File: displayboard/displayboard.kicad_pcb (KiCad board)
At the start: 2 copper layers, 103 x 41 mm, 2 parts, among them P2 CONN_01X08, P3 CONN_01X08

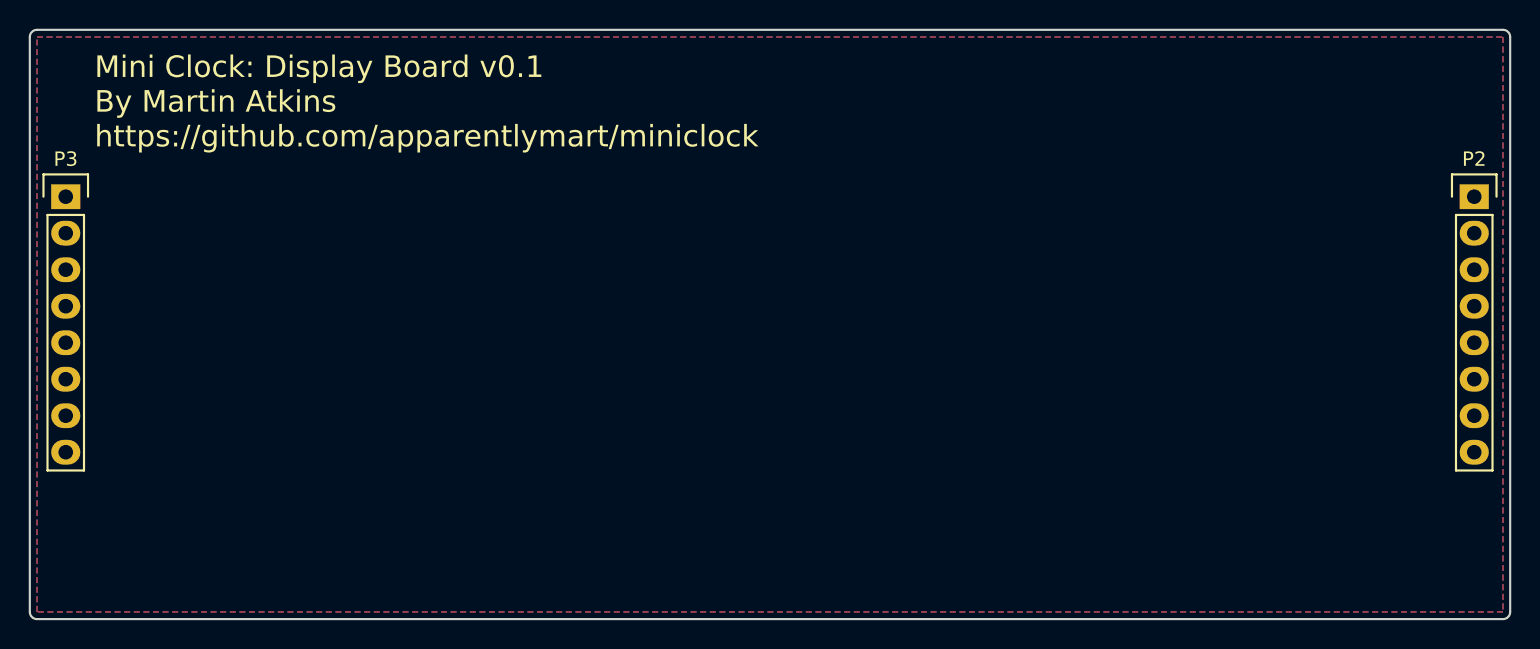
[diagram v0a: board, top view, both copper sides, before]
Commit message: PCB footprint assignment and floor planning.
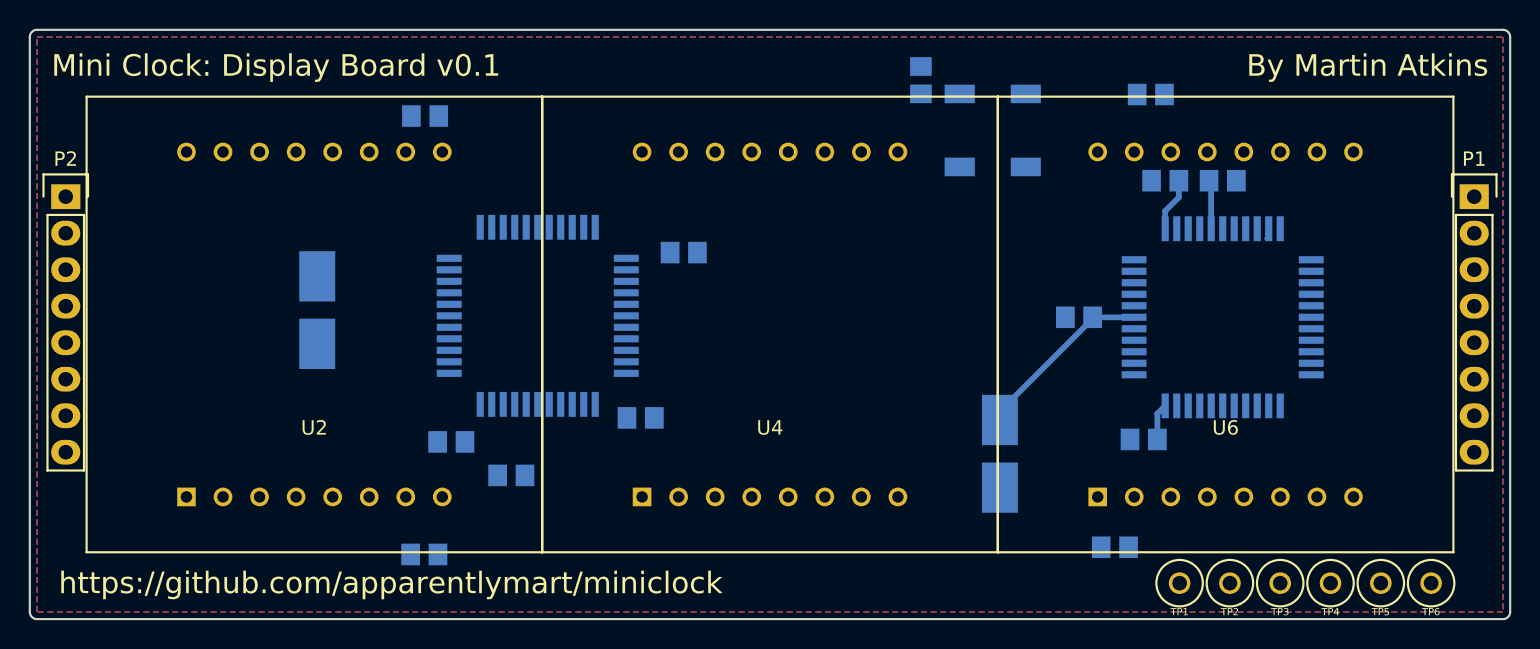
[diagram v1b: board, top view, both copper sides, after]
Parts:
- added C1: 0.1u, miniclock:0805, B.Cu at (10.5, -17.0)
- added C10: 0.1u, miniclock:0805, B.Cu at (26.0, 8.00)
- added C11: 47uF, miniclock:UWX1V470MCL1GB, B.Cu at (16.0, 9.00)
- added C2: 0.1u, miniclock:0805, B.Cu at (-22.2, 8.17)
- added C3: 0.1u, miniclock:0805, B.Cu at (-18.0, 10.5)
- added C4: 0.1u, miniclock:0805, B.Cu at (-6.00, -5.00)
- added C5: 0.1u, miniclock:0805, B.Cu at (-9.00, 6.50)
- added C6: 47uF, miniclock:UWX1V470MCL1GB, B.Cu at (-31.5, -1.00)
- added C7: 0.1u, miniclock:0805, B.Cu at (31.5, -10.0)
- added C8: 0.1u, miniclock:0805, B.Cu at (21.5, -0.50)
- added C9: 0.1u, miniclock:0805, B.Cu at (27.5, -10.0)
- added JP1: Jumper_NO_Small, miniclock:0805, B.Cu at (-24.1, 16.0)
- added JP2: Jumper_NO_Small, miniclock:0805, B.Cu at (-24.0, -14.5)
- added JP3: Jumper_NO_Small, miniclock:0805, B.Cu at (24.0, 15.5)
- added JP4: Jumper_NO_Small, miniclock:0805, B.Cu at (26.5, -16.0)
- added TP1: TESTPOINT, miniclock:TESTPOINT, F.Cu at (28.5, 18.0)
- added TP2: TESTPOINT, miniclock:TESTPOINT, F.Cu at (32.0, 18.0)
- added TP3: TESTPOINT, miniclock:TESTPOINT, F.Cu at (35.5, 18.0)
- added TP4: TESTPOINT, miniclock:TESTPOINT, F.Cu at (39.0, 18.0)
- added TP5: TESTPOINT, miniclock:TESTPOINT, F.Cu at (42.5, 18.0)
- added TP6: TESTPOINT, miniclock:TESTPOINT, F.Cu at (46.0, 18.0)
- added U1: SG-636PCE, miniclock:SG-636PCE, B.Cu at (15.5, -13.5)
- added U2: LEDM, miniclock:KWM-R30881CUYB, F.Cu at (-31.7, 0.00)
- added U3: MAX6960, miniclock:MAX6960, B.Cu at (-16.2, -0.60)
- added U4: LEDM, miniclock:KWM-R30881CUYB, F.Cu at (0.00, 0.00)
- added U5: MAX6960, miniclock:MAX6960, B.Cu at (31.5, -0.50)
- added U6: LEDM, miniclock:KWM-R30881CUYB, F.Cu at (31.7, 0.00)
- renumbered P2 to P1, P3 to P2
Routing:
- net +3V3: track 0.00 -> 22.4 mm
- net MOSI: track 0.90 -> 0.00 mm
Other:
- board text added: "By Martin Atkins"
- board text added: "Mini Clock: Display Board v0.1"
- board text added: "https://github.com/apparentlymart/miniclock"
- board text removed: "Mini Clock: Display Board v0.1 By Martin Atkins https://github.com/apparentlymart/miniclock"

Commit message: Spinning the chips around trying to find the least-sucky orientation.
There seems to be no good orientation for these chips vs. the pinout of
the LED displays.
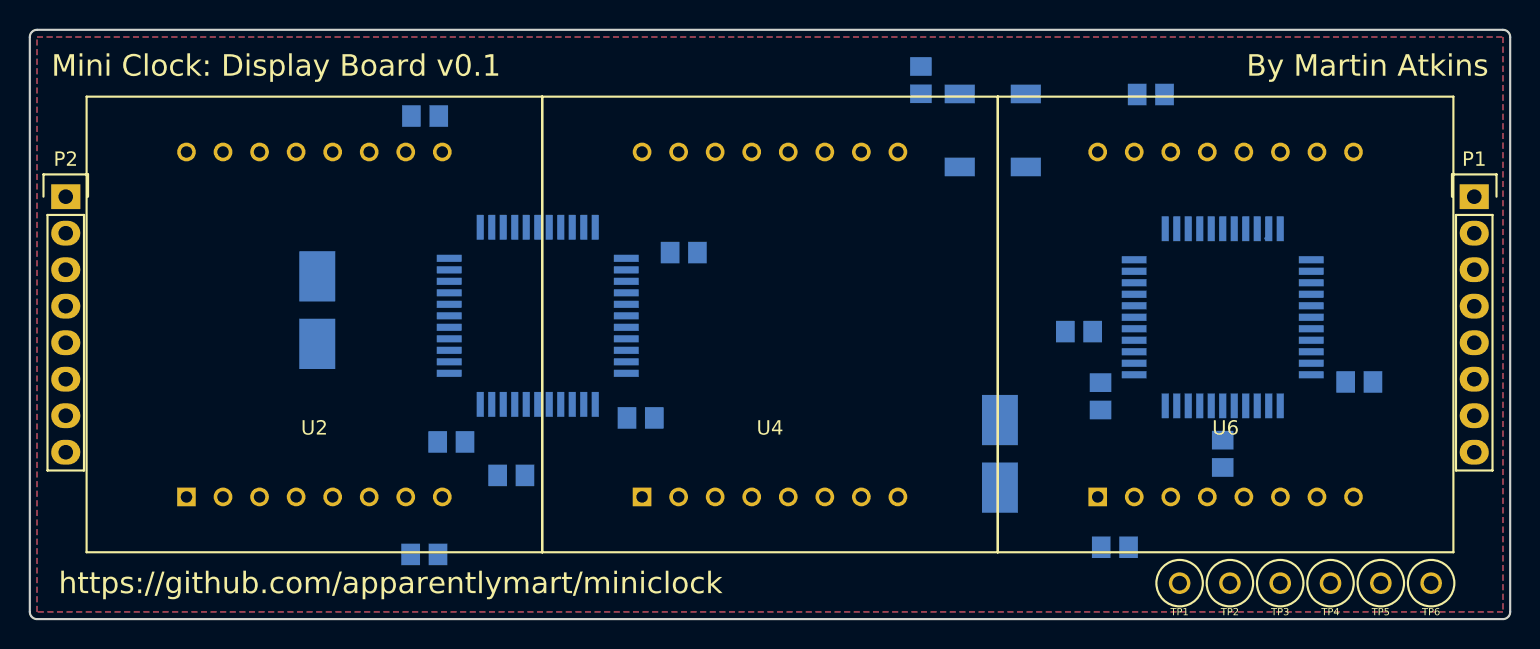
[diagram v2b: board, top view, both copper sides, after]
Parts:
- moved C7 16.9 mm to (41.0, 4.00)
- moved C9 12.1 mm to (21.5, 0.50)
- moved C8 5.70 mm to (23.0, 5.00), turned to 270 degrees
- moved C10 5.59 mm to (31.5, 9.00), turned to 270 degrees
- turned U3 to 270 degrees
- turned U5 to 270 degrees
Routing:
- net +3V3: track 22.4 -> 0.60 mm

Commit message: Thin the LED anode/cathode traces.
They were originally classified as power but the PCB is too crowded to
give them thick power traces, and the thin signal traces should do well
enough since we're not going to be drawing more than 20mA per LED anyway.
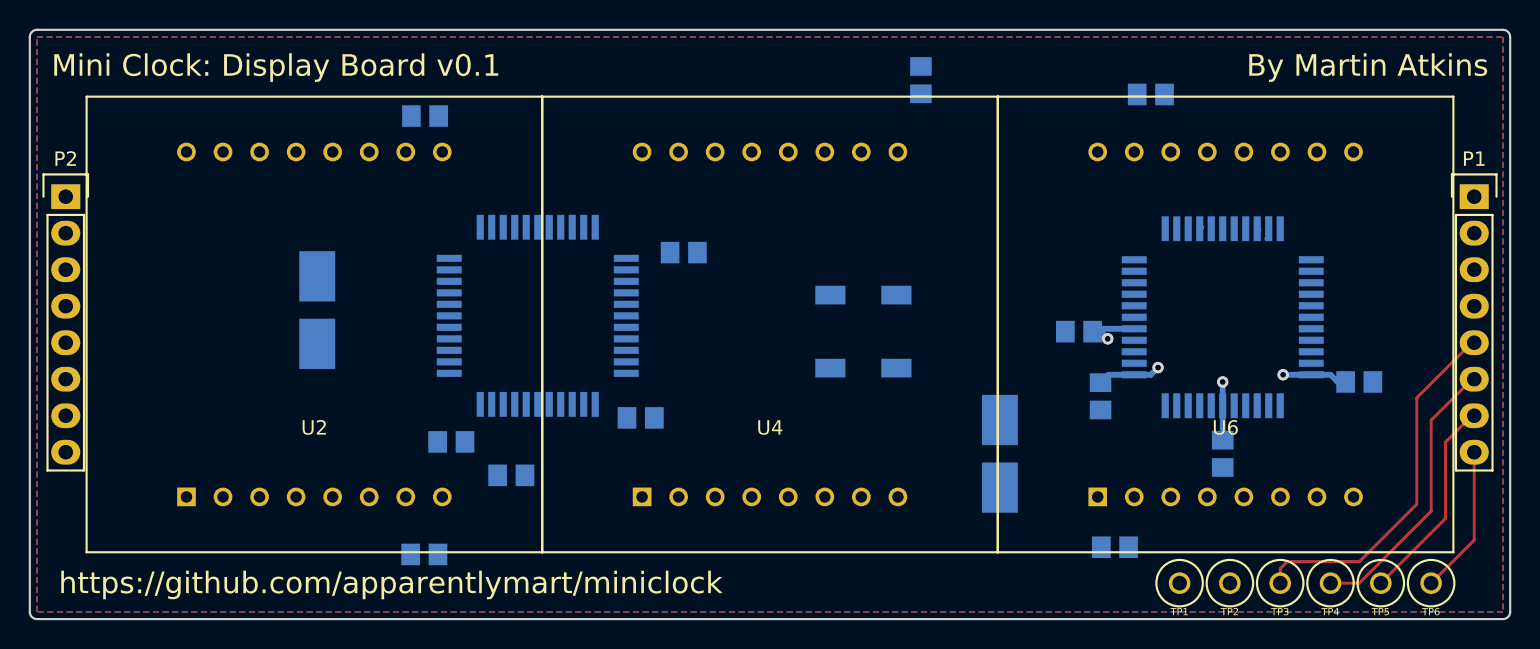
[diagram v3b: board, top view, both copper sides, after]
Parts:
- moved U1 16.6 mm to (6.50, 0.50)
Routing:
- net SCLK: track 0.15 -> 25.5 mm
- net MOSI: track 0.00 -> 19.6 mm
- net +3V3: track 0.60 -> 17.9 mm, vias 0 -> 4
- net MISO: track 0.15 -> 14.4 mm
- net SSEL: track 0.15 -> 10.5 mm
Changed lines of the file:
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@@
   (general
     (links 120)
-    (no_connects 91)
-    (area -51.575001 -20.575001 51.575001 20.575001)
+    (no_connects 79)
+    (area -51.575001 -20.575001 51.575001 20.6)
     (thickness 1.6)
     (drawings 11)
-    (tracks 7)
+    (tracks 47)
     (zones 0)
     (modules 29)
@@
     (uvia_drill 0.1)
     (add_net ADDCLK)
-    (add_net MISO)
-    (add_net MOSI)
-    (add_net "Net-(JP1-Pad2)")
-    (add_net "Net-(JP2-Pad1)")
-    (add_net "Net-(JP3-Pad2)")
-    (add_net "Net-(JP4-Pad1)")
-    (add_net "Net-(P2-Pad1)")
-    (add_net "Net-(P2-Pad2)")
-    (add_net "Net-(P2-Pad3)")
-    (add_net "Net-(P2-Pad4)")
-    (add_net "Net-(P2-Pad5)")
-    (add_net "Net-(P2-Pad6)")
-    (add_net "Net-(P2-Pad7)")
-    (add_net "Net-(P2-Pad8)")
-    (add_net "Net-(U1-Pad1)")
-    (add_net "Net-(U3-Pad39)")
-    (add_net "Net-(U5-Pad29)")
-    (add_net "Net-(U5-Pad30)")
-    (add_net "Net-(U5-Pad31)")
-    (add_net "Net-(U5-Pad32)")
-    (add_net "Net-(U5-Pad33)")
-    (add_net "Net-(U5-Pad35)")
-    (add_net "Net-(U5-Pad36)")
-    (add_net "Net-(U5-Pad37)")
-    (add_net "Net-(U5-Pad39)")
-    (add_net OSC)
-    (add_net SCLK)
-    (add_net SSEL)
-    (add_net ~RESET)
-  )
-  (net_class Power ""
-    (clearance 0.2)
-    (trace_width 0.4)
-    (via_dia 0.8)
-    (via_drill 0.4)
-    (uvia_dia 0.3)
-    (uvia_drill 0.1)
-    (add_net +3V3)
     (add_net D0_C1)
     (add_net D0_C2)
@@
     (add_net D2_R7)
     (add_net D2_R8)
+    (add_net MISO)
+    (add_net MOSI)
+    (add_net "Net-(JP1-Pad2)")
+    (add_net "Net-(JP2-Pad1)")
+    (add_net "Net-(JP3-Pad2)")
+    (add_net "Net-(JP4-Pad1)")
+    (add_net "Net-(P2-Pad1)")
+    (add_net "Net-(P2-Pad2)")
+    (add_net "Net-(P2-Pad3)")
+    (add_net "Net-(P2-Pad4)")
+    (add_net "Net-(P2-Pad5)")
+    (add_net "Net-(P2-Pad6)")
+    (add_net "Net-(P2-Pad7)")
+    (add_net "Net-(P2-Pad8)")
+    (add_net "Net-(U1-Pad1)")
+    (add_net "Net-(U3-Pad39)")
+    (add_net "Net-(U5-Pad29)")
+    (add_net "Net-(U5-Pad30)")
+    (add_net "Net-(U5-Pad31)")
+    (add_net "Net-(U5-Pad32)")
+    (add_net "Net-(U5-Pad33)")
+    (add_net "Net-(U5-Pad35)")
+    (add_net "Net-(U5-Pad36)")
+    (add_net "Net-(U5-Pad37)")
+    (add_net "Net-(U5-Pad39)")
+    (add_net OSC)
+    (add_net SCLK)
+    (add_net SSEL)
+    (add_net ~RESET)
+  )
+  (net_class Power ""
+    (clearance 0.2)
+    (trace_width 0.4)
+    (via_dia 0.8)
+    (via_drill 0.4)
+    (uvia_dia 0.3)
+    (uvia_drill 0.1)
+    (add_net +3V3)
     (add_net GND)
   )
@@
   )
   (module miniclock:SG-636PCE (layer B.Cu)
-    (at 15.5 -13.5 90)
+    (at 6.5 0.5 90)
     (fp_text reference U1 (at 0 3.25 90) (layer B.SilkS)
       (effects (font (size 1 1) (thickness 0.15)) (justify mirror))
@@
   (gr_line (start -51 20.5) (end 51 20.5) (layer Edge.Cuts) (width 0.15))
   (gr_line (start -51.5 -20) (end -51.5 20) (layer Edge.Cuts) (width 0.15))
+  (segment (start 35.69999 3.49999) (end 35.69998 3.5) (width 0.4) (layer B.Cu) (net 2))
+  (segment (start 37.66 3.49999) (end 35.69999 3.49999) (width 0.4) (layer B.Cu) (net 2) (status 10))
+  (via (at 35.69998 3.5) (size 0.8) (drill 0.4) (layers F.Cu B.Cu) (net 2))
+  (segment (start 31.499995 4.000021) (end 31.499974 4) (width 0.4) (layer B.Cu) (net 2))
+  (segment (start 31.499995 5.66) (end 31.499995 4.000021) (width 0.4) (layer B.Cu) (net 2) (status 10))
+  (via (at 31.499974 4) (size 0.8) (drill 0.4) (layers F.Cu B.Cu) (net 2))
+  (segment (start 22.45 0.5) (end 23 0.5) (width 0.4) (layer B.Cu) (net 2) (status 30))
+  (via (at 23.5 1) (size 0.8) (drill 0.4) (layers F.Cu B.Cu) (net 2))
+  (segment (start 23 0.5) (end 23.5 1) (width 0.4) (layer B.Cu) (net 2) (status 10))
+  (segment (start 25.34 3.49999) (end 26.50001 3.49999) (width 0.4) (layer B.Cu) (net 2) (status 10))
+  (segment (start 26.50001 3.49999) (end 27 3) (width 0.4) (layer B.Cu) (net 2))
+  (via (at 27 3) (size 0.8) (drill 0.4) (layers F.Cu B.Cu) (net 2))
+  (segment (start 31.499995 5.66) (end 31.499995 8.049995) (width 0.4) (layer B.Cu) (net 2) (status 30))
+  (segment (start 31.499995 8.049995) (end 31.5 8.05) (width 0.4) (layer B.Cu) (net 2) (status 30))
+  (segment (start 25.34 0.299994) (end 22.650006 0.299994) (width 0.4) (layer B.Cu) (net 2) (status 30))
+  (segment (start 22.650006 0.299994) (end 22.45 0.5) (width 0.4) (layer B.Cu) (net 2) (status 30))
+  (segment (start 25.34 3.49999) (end 23.55001 3.49999) (width 0.4) (layer B.Cu) (net 2) (status 30))
+  (segment (start 23.55001 3.49999) (end 23 4.05) (width 0.4) (layer B.Cu) (net 2) (status 30))
+  (segment (start 39.5 4) (end 38.99999 3.49999) (width 0.4) (layer B.Cu) (net 2) (status 10))
+  (segment (start 38.99999 3.49999) (end 37.66 3.49999) (width 0.4) (layer B.Cu) (net 2) (status 20))
+  (segment (start 40.05 4) (end 39.5 4) (width 0.4) (layer B.Cu) (net 2) (status 30))
   (segment (start 16 6.65) (end 16 6.05) (width 0.4) (layer B.Cu) (net 2) (status 30))
   (segment (start 48.8476 -8.89) (end 49 -8.89) (width 0.2) (layer F.Cu) (net 3) (status 30))
+  (segment (start 49 1.27) (end 48.8476 1.27) (width 0.2) (layer F.Cu) (net 4) (status 30))
+  (segment (start 48.8476 1.27) (end 45 5.1176) (width 0.2) (layer F.Cu) (net 4) (status 10))
+  (segment (start 45 5.1176) (end 45 12.5) (width 0.2) (layer F.Cu) (net 4))
+  (segment (start 41 16.5) (end 36 16.5) (width 0.2) (layer F.Cu) (net 4))
+  (segment (start 45 12.5) (end 41 16.5) (width 0.2) (layer F.Cu) (net 4))
+  (segment (start 36 16.5) (end 35.5 17) (width 0.2) (layer F.Cu) (net 4))
+  (segment (start 35.5 17) (end 35.5 18) (width 0.2) (layer F.Cu) (net 4) (status 20))
   (segment (start 48.8476 1.27) (end 49 1.27) (width 0.2) (layer B.Cu) (net 4) (status 30))
+  (segment (start 46 13) (end 41 18) (width 0.2) (layer F.Cu) (net 5))
+  (segment (start 41 18) (end 39 18) (width 0.2) (layer F.Cu) (net 5) (status 20))
+  (segment (start 46 6.6576) (end 46 13) (width 0.2) (layer F.Cu) (net 5))
+  (segment (start 49 3.81) (end 48.8476 3.81) (width 0.2) (layer F.Cu) (net 5) (status 30))
+  (segment (start 48.8476 3.81) (end 46 6.6576) (width 0.2) (layer F.Cu) (net 5) (status 10))
+  (segment (start 47 8.1976) (end 47 13.5) (width 0.2) (layer F.Cu) (net 6))
+  (segment (start 47 13.5) (end 42.5 18) (width 0.2) (layer F.Cu) (net 6) (status 20))
+  (segment (start 48.8476 6.35) (end 47 8.1976) (width 0.2) (layer F.Cu) (net 6) (status 10))
   (segment (start 48.8476 6.35) (end 49 6.35) (width 0.2) (layer F.Cu) (net 6) (status 30))
+  (segment (start 49 8.89) (end 49 15) (width 0.2) (layer F.Cu) (net 7) (status 10))
+  (segment (start 49 15) (end 46 18) (width 0.2) (layer F.Cu) (net 7) (status 20))
   (segment (start 48.8476 8.89) (end 49 8.89) (width 0.2) (layer F.Cu) (net 7) (status 30))
+  (segment (start 30 -6.760003) (end 29.899997 -6.66) (width 0.4) (layer B.Cu) (net 49) (status 30))
   (segment (start 34.487151 -5.987151) (end 34.724405 -5.987151) (width 0.2) (layer B.Cu) (net 52) (status 30))
+  (segment (start 33.987141 -6.572851) (end 33.899992 -6.66) (width 0.4) (layer B.Cu) (net 53) (status 30))
   (segment (start 25.339995 -0.5) (end 25.34 -0.500005) (width 0.4) (layer B.Cu) (net 71) (status 30))
   (zone (net 1) (net_name GND) (layer B.Cu) (hatch edge 0.508)

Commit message: Connect the bulk capacitor.
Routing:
- net +3V3: track 17.9 -> 27.2 mm
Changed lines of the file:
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@@
     (thickness 1.6)
     (drawings 11)
-    (tracks 47)
+    (tracks 51)
     (zones 0)
     (modules 29)
@@
   (gr_line (start -51 20.5) (end 51 20.5) (layer Edge.Cuts) (width 0.15))
   (gr_line (start -51.5 -20) (end -51.5 20) (layer Edge.Cuts) (width 0.15))
+  (segment (start 16 6.65) (end 16 4.5) (width 0.4) (layer B.Cu) (net 2))
+  (segment (start 21.85 4.05) (end 23 4.05) (width 0.4) (layer B.Cu) (net 2))
+  (segment (start 16 4.5) (end 16.45 4.05) (width 0.4) (layer B.Cu) (net 2))
+  (segment (start 16.45 4.05) (end 21.85 4.05) (width 0.4) (layer B.Cu) (net 2))
   (segment (start 35.69999 3.49999) (end 35.69998 3.5) (width 0.4) (layer B.Cu) (net 2))
   (segment (start 37.66 3.49999) (end 35.69999 3.49999) (width 0.4) (layer B.Cu) (net 2) (status 10))
